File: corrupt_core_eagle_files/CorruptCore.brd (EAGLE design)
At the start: 100 x 58 mm, 90 parts, among them K1 DTS-3, K10 DTS-3, K11 DTS-3, K12 DTS-3, K13 DTS-3, K14 DTS-3, K15 DTS-3, K16 DTS-3, K2 DTS-3, K3 DTS-3, K4 DTS-3, K5 DTS-3, K6 DTS-3, K7 DTS-3, K8 DTS-3, K9 DTS-3, U1 MEGA8-P, U2 SNX4HC595SOIC16, U3 SNX4HC595SOIC16, U4 SNX4HC595SOIC16, U5 ULN2803ASOIC18, U6 ULN2803ASOIC18, U7 ULN2803ASOIC18, U8 LTC1799, Y1 16MHz

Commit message: -more silkscreen changes
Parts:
- removed 5V@FREQ, FP1, FP2, FREQ, GND@FREQ: (no value), wirepad:1,6/0,8
- removed FREQSET: user, resistor:0207/7
- added 5V@CLK, CLK_OUT, CPT1, CPT2, GND@CLK: (no value), wirepad:1,6/0,8
- added CLKSET: user, resistor:0207/7
- moved U8 10.2 mm to (89.0, 37.5)
- moved DIV 9.00 mm to (87.8, 43.5), turned to 0 degrees
- moved 5V@POT1 2.46 mm to (98.2, 31.5)
- moved 5V@POT2 2.46 mm to (98.2, 22.0)
- moved 5V@POT3 2.46 mm to (98.2, 12.5)
- moved GND@POT1 2.46 mm to (98.2, 26.5)
- moved GND@POT2 2.46 mm to (98.2, 17.0)
- moved GND@POT3 2.46 mm to (98.2, 7.50)
- moved POT1 2.46 mm to (98.2, 29.0)
- moved POT2 2.46 mm to (98.2, 19.5)
- moved POT3 2.46 mm to (98.2, 10.0)
- moved T1 2.02 mm to (47.0, 46.2)
- moved T2 2.02 mm to (47.0, 42.2)
- moved T3 2.02 mm to (47.0, 38.2)
- moved T4 2.02 mm to (47.0, 34.2)
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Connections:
- net +5V: now also 5V@CLK.1, CPT1.1; no longer 5V@FREQ.1, FP1.1
- net GND: now also GND@CLK.1; no longer GND@FREQ.1
- net N$14: now also CLKSET.1, CPT2.1; no longer FP2.1, FREQSET.1
- net N$16: now also CLKSET.2; no longer FREQSET.2
- net N$5: now also CLK_OUT.1; no longer FREQ.1
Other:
- board text added: "Bank 1"
- board text added: "Bank 2"
- board text added: "Bank 3"
- board text added: "CLK OUT"
- board text added: "Quick Bank"
- board text removed: "Bus 1"

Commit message: -made the shitty meme worse
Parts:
- moved R1 6.26 mm to (13.0, 12.0), turned to 0 degrees
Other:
- outline, holes or cut-outs redrawn

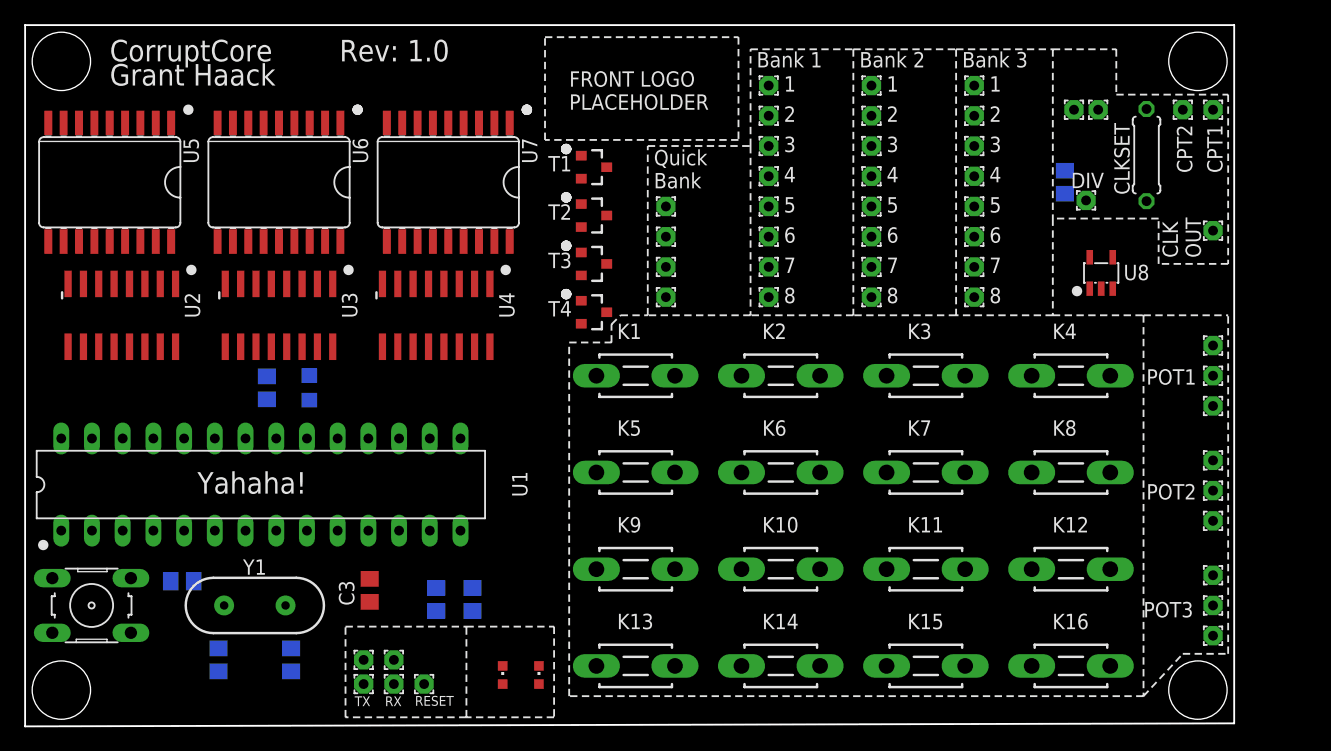
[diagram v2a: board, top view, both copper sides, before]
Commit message: -added dimensions -added DRC for Elecrow boardhouse -pretty much done with silkscreen
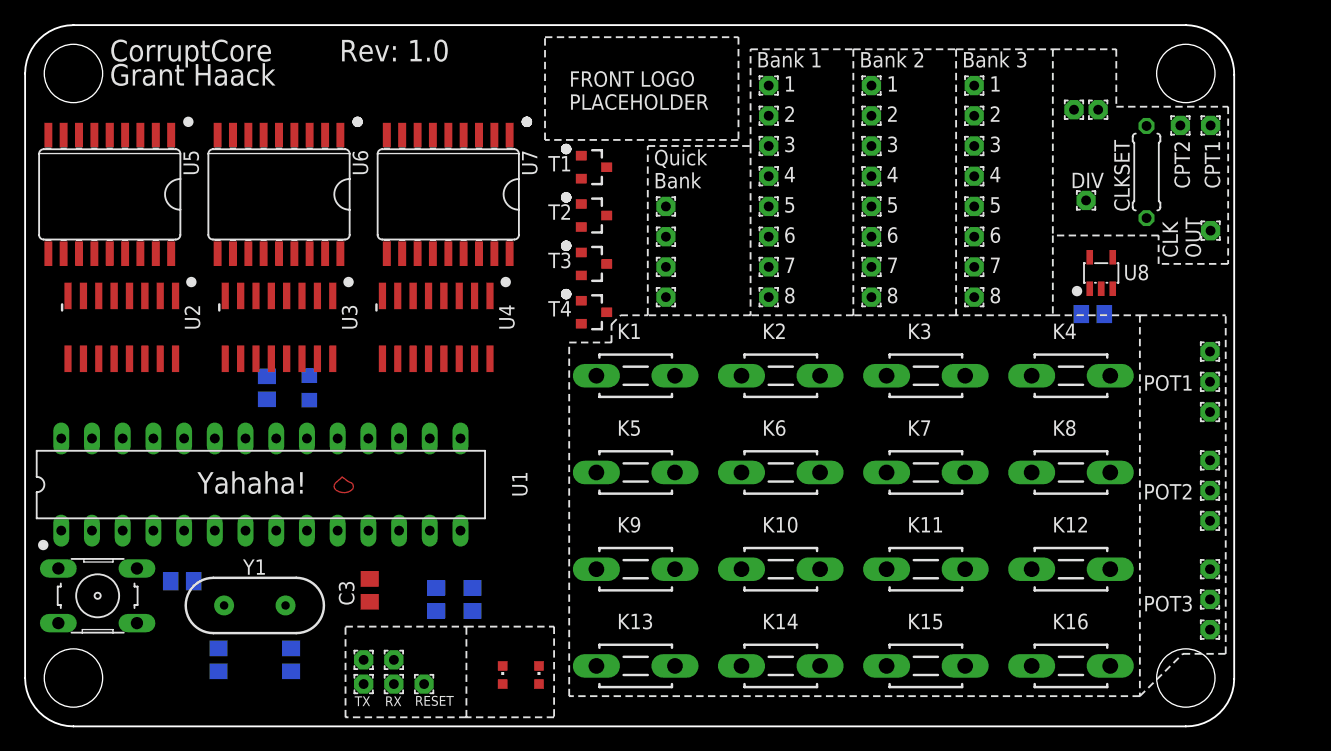
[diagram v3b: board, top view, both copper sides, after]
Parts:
- moved C5 11.1 mm to (88.3, 34.1), turned to 180 degrees
- moved CLKSET 1.40 mm to (92.8, 45.9)
- moved CPT1 1.32 mm to (98.0, 49.7)
- moved CPT2 1.32 mm to (95.5, 49.7)
- moved U2 1.00 mm to (8.00, 33.0)
- moved U3 1.00 mm to (21.0, 33.0)
- moved U4 1.00 mm to (34.0, 33.0)
- moved U5 1.00 mm to (7.00, 44.0)
- moved U6 1.00 mm to (21.0, 44.0)
- moved U7 1.00 mm to (35.0, 44.0)
- moved S1 0.94 mm to (6.00, 10.8)
- moved 5V@POT1 0.56 mm to (98.0, 31.0)
- moved 5V@POT3 0.56 mm to (98.0, 13.0)
- moved GND@POT1 0.56 mm to (98.0, 26.0)
- moved GND@POT3 0.56 mm to (98.0, 8.00)
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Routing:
- added copper zone on layer 1, net N$15
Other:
- outline, holes or cut-outs redrawn
